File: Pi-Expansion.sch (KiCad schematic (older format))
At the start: 14 parts, among them J1 RPi_GPIO, J2 MMCX_H, P1 BATT, U1 A2200-A, U2 SPX2920U-5.0

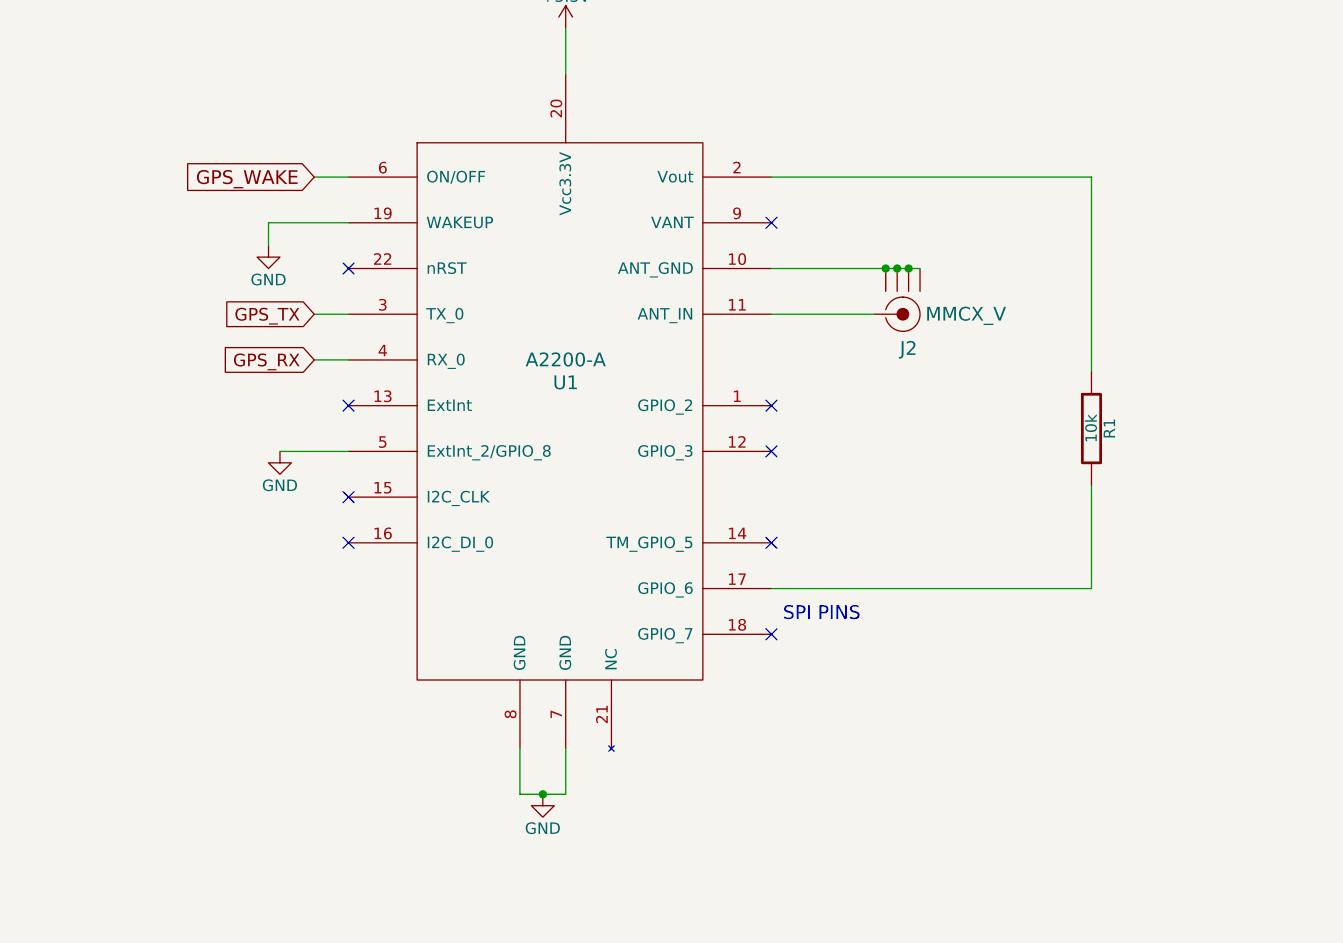
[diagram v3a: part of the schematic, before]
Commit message: Updated layout around gps, reconfigured for autowakeup and NMEA at 4800.
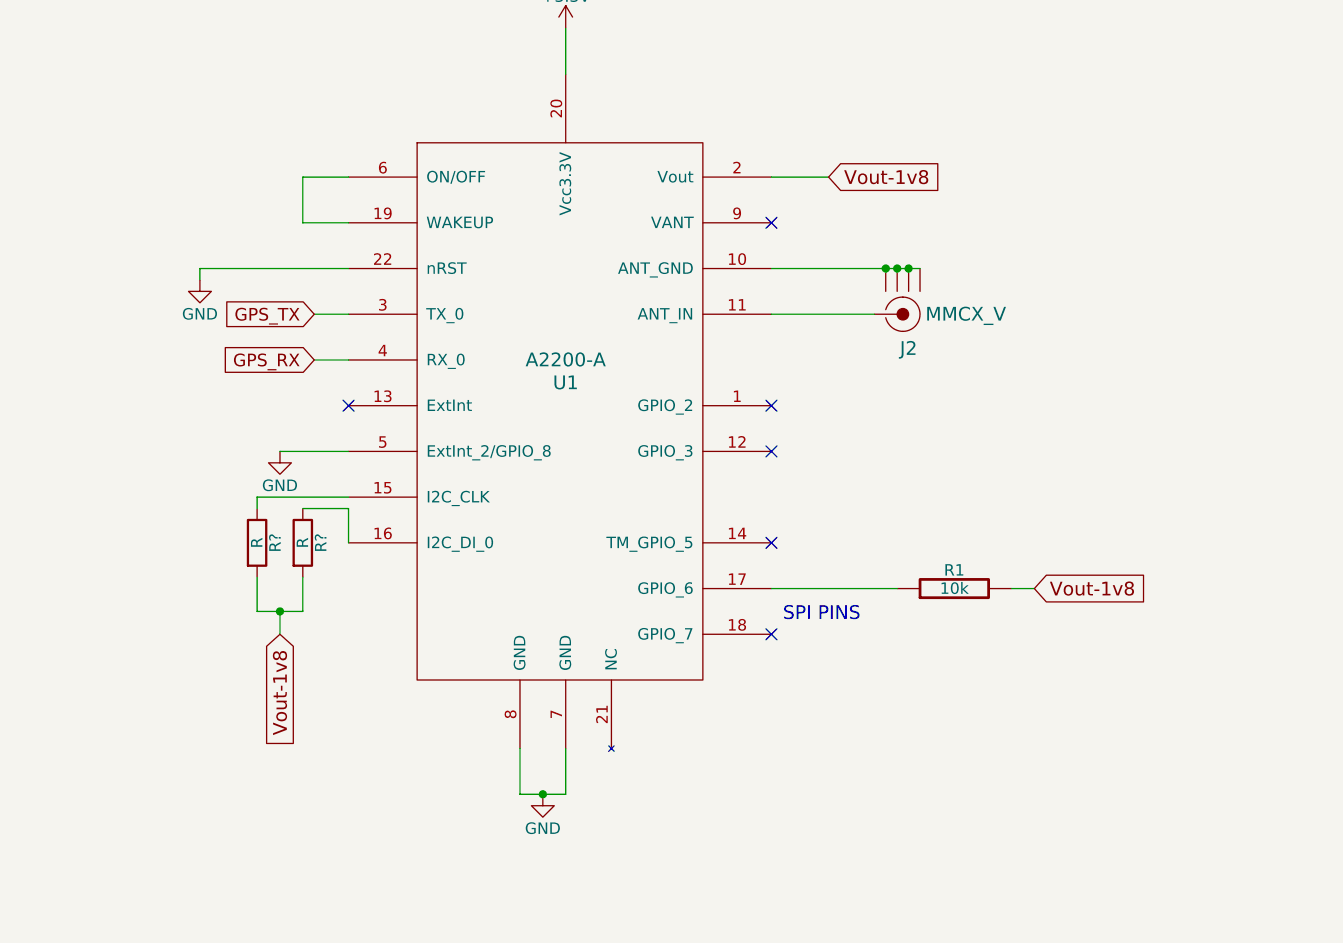
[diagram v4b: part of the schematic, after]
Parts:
- added R? (x2): R, symbol R
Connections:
- net GND: now also U1.22 (nRST); no longer U1.19 (WAKEUP)
- net GPS_WAKE: no longer U1.6 (ON/OFF)
- net at U1.15 (I2C_CLK): now also R?.1
- net at U1.16 (I2C_DI_0): now also R?.1
- net at U1.17 (GPIO_6): now also R1.1; no longer R1.2
- net Vout-1v8: now reaches U1.2 (Vout)
- net Vout-1v8: now also R1.2, R?.2, R?.2; no longer R1.1
- new net: U1.19 (WAKEUP), U1.6 (ON/OFF)
- no-connect marks 29 -> 26
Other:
- moved on the sheet: R1
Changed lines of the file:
@@
 L R-RESCUE-Pi-Expansion R1
 U 1 1 56C04659
-P 5650 2600
-F 0 "R1" V 5730 2600 50  0000 C CNN
-F 1 "10k" V 5650 2600 50  0000 C CNN
-F 2 "FT:1206" H 5650 2600 60  0001 C CNN
-F 3 "" H 5650 2600 60  0000 C CNN
-	1    5650 2600
-	1    0    0    -1
+P 5050 3300
+F 0 "R1" V 5130 3300 50  0000 C CNN
+F 1 "10k" V 5050 3300 50  0000 C CNN
+F 2 "FT:1206" H 5050 3300 60  0001 C CNN
+F 3 "" H 5050 3300 60  0000 C CNN
+	1    5050 3300
+	0    -1   -1   0
 $EndComp
 Wire Wire Line
@@
 Wire Wire Line
 	2100 2700 2400 2700
-Wire Wire Line
-	4250 1500 5650 1500
-Wire Wire Line
-	5650 1500 5650 2350
-Wire Wire Line
-	4250 3300 5650 3300
-Wire Wire Line
-	5650 3300 5650 2850
 Text Notes 4300 3450 0    60   ~ 0
 SPI PINS
@@
 NoConn ~ 4250 2500
 NoConn ~ 2400 2500
-NoConn ~ 2400 2900
-NoConn ~ 2400 3100
 NoConn ~ 4250 1700
 NoConn ~ 3400 5400
-NoConn ~ 2400 1900
 Text GLabel 3750 5700 2    60   Input ~ 0
 GPS_WAKE
 Wire Wire Line
 	3400 5700 3750 5700
-Text GLabel 2250 1500 0    60   Input ~ 0
-GPS_WAKE
-Wire Wire Line
-	2400 1500 2250 1500
-$Comp
-L GND #PWR010
-U 1 1 56C26D35
-P 2050 1800
-F 0 "#PWR010" H 2050 1550 50  0001 C CNN
-F 1 "GND" H 2050 1650 50  0000 C CNN
-F 2 "" H 2050 1800 50  0000 C CNN
-F 3 "" H 2050 1800 50  0000 C CNN
-	1    2050 1800
-	1    0    0    -1
-$EndComp
-Wire Wire Line
-	2050 1800 2050 1700
-Wire Wire Line
-	2050 1700 2400 1700
 NoConn ~ 1500 5900
 NoConn ~ 1500 5800
@@
 Wire Wire Line
 	8750 1450 9800 1450
+Wire Wire Line
+	2400 1700 2200 1700
+Wire Wire Line
+	2200 1700 2200 1500
+Wire Wire Line
+	2200 1500 2400 1500
+$Comp
+L R R?
+U 1 1 573A3BBE
+P 2200 3100
+F 0 "R?" V 2280 3100 50  0000 C CNN
+F 1 "R" V 2200 3100 50  0000 C CNN
+F 2 "" V 2130 3100 50  0000 C CNN
+F 3 "" H 2200 3100 50  0000 C CNN
+	1    2200 3100
+	1    0    0    -1
+$EndComp
+$Comp
+L R R?
+U 1 1 573A3C2D
+P 2000 3100
+F 0 "R?" V 2080 3100 50  0000 C CNN
+F 1 "R" V 2000 3100 50  0000 C CNN
+F 2 "" V 1930 3100 50  0000 C CNN
+F 3 "" H 2000 3100 50  0000 C CNN
+	1    2000 3100
+	1    0    0    -1
+$EndComp
+Wire Wire Line
+	2400 2900 2000 2900
+Wire Wire Line
+	2000 2900 2000 2950
+Wire Wire Line
+	2400 3100 2400 2950
+Wire Wire Line
+	2400 2950 2200 2950
+Wire Wire Line
+	2000 3250 2000 3400
+Wire Wire Line
+	2000 3400 2200 3400
+Wire Wire Line
+	2200 3400 2200 3250
+Text GLabel 2100 3500 3    60   Input ~ 0
+Vout-1v8
+Text GLabel 4500 1500 2    60   Input ~ 0
+Vout-1v8
+Text GLabel 5400 3300 2    60   Input ~ 0
+Vout-1v8
+Wire Wire Line
+	2100 3500 2100 3400
+Connection ~ 2100 3400
+Wire Wire Line
+	4250 1500 4500 1500
+Wire Wire Line
+	4250 3300 4800 3300
+Wire Wire Line
+	5300 3300 5400 3300
+$Comp
+L GND #PWR?
+U 1 1 573A4B6B
+P 1750 1950
+F 0 "#PWR?" H 1750 1700 50  0001 C CNN
+F 1 "GND" H 1750 1800 50  0000 C CNN
+F 2 "" H 1750 1950 50  0000 C CNN
+F 3 "" H 1750 1950 50  0000 C CNN
+	1    1750 1950
+	1    0    0    -1
+$EndComp
+Wire Wire Line
+	2400 1900 1750 1900
+Wire Wire Line
+	1750 1900 1750 1950
 $EndSCHEMATC

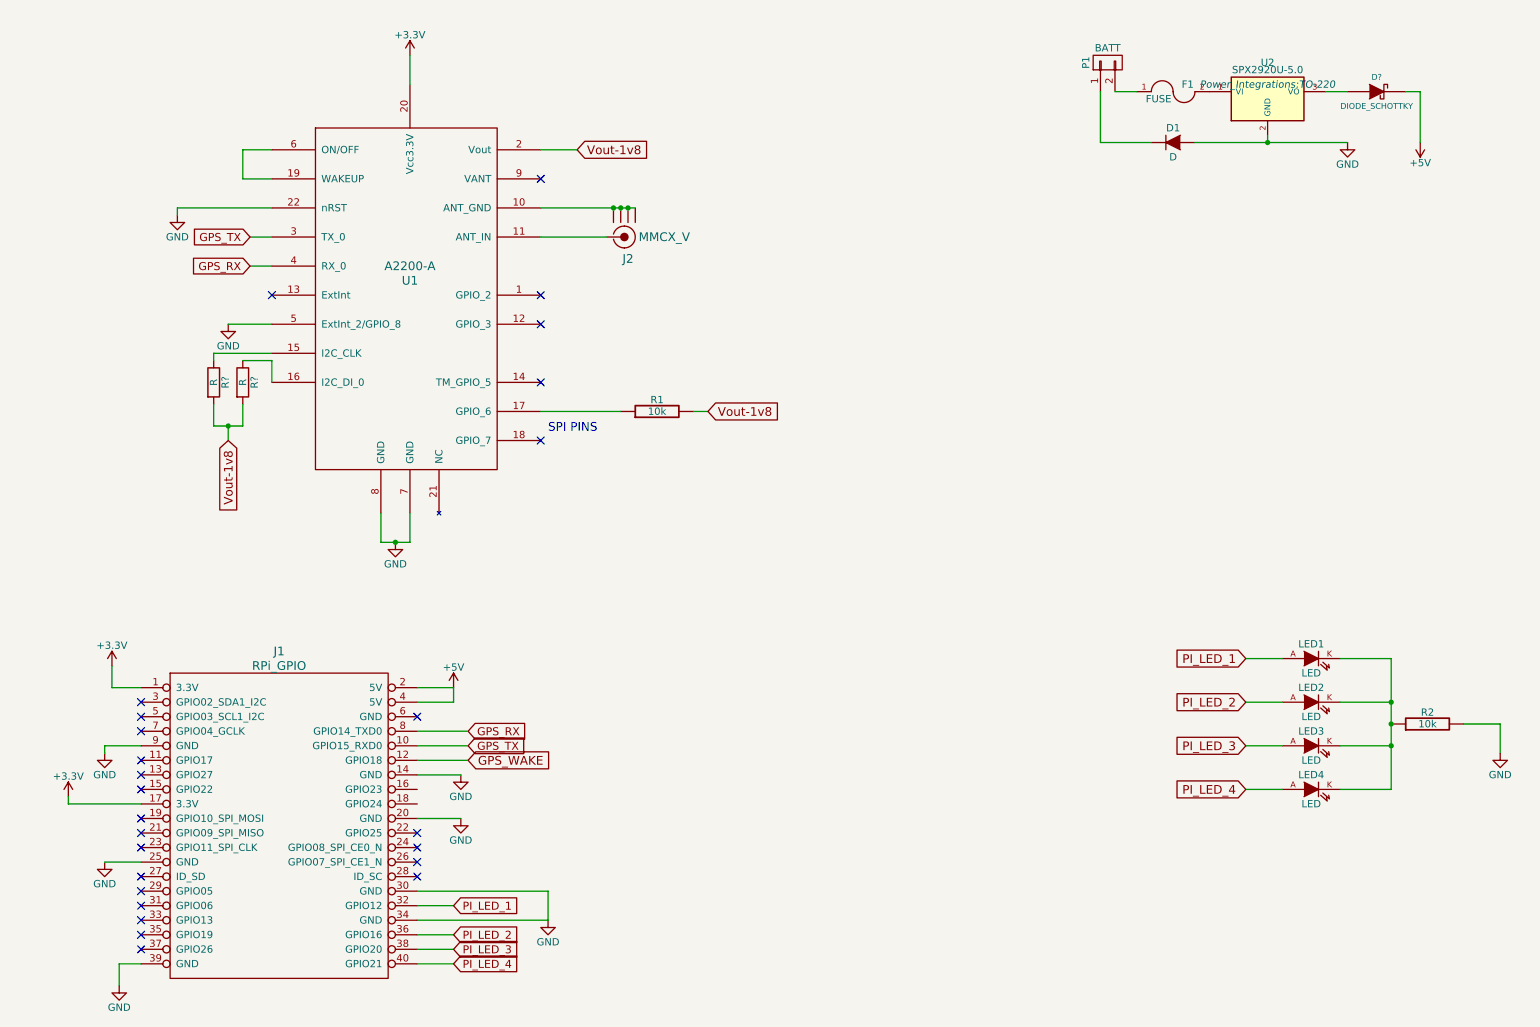
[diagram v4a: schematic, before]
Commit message: minor tweaks, and rotated pi header, removed infill and traces
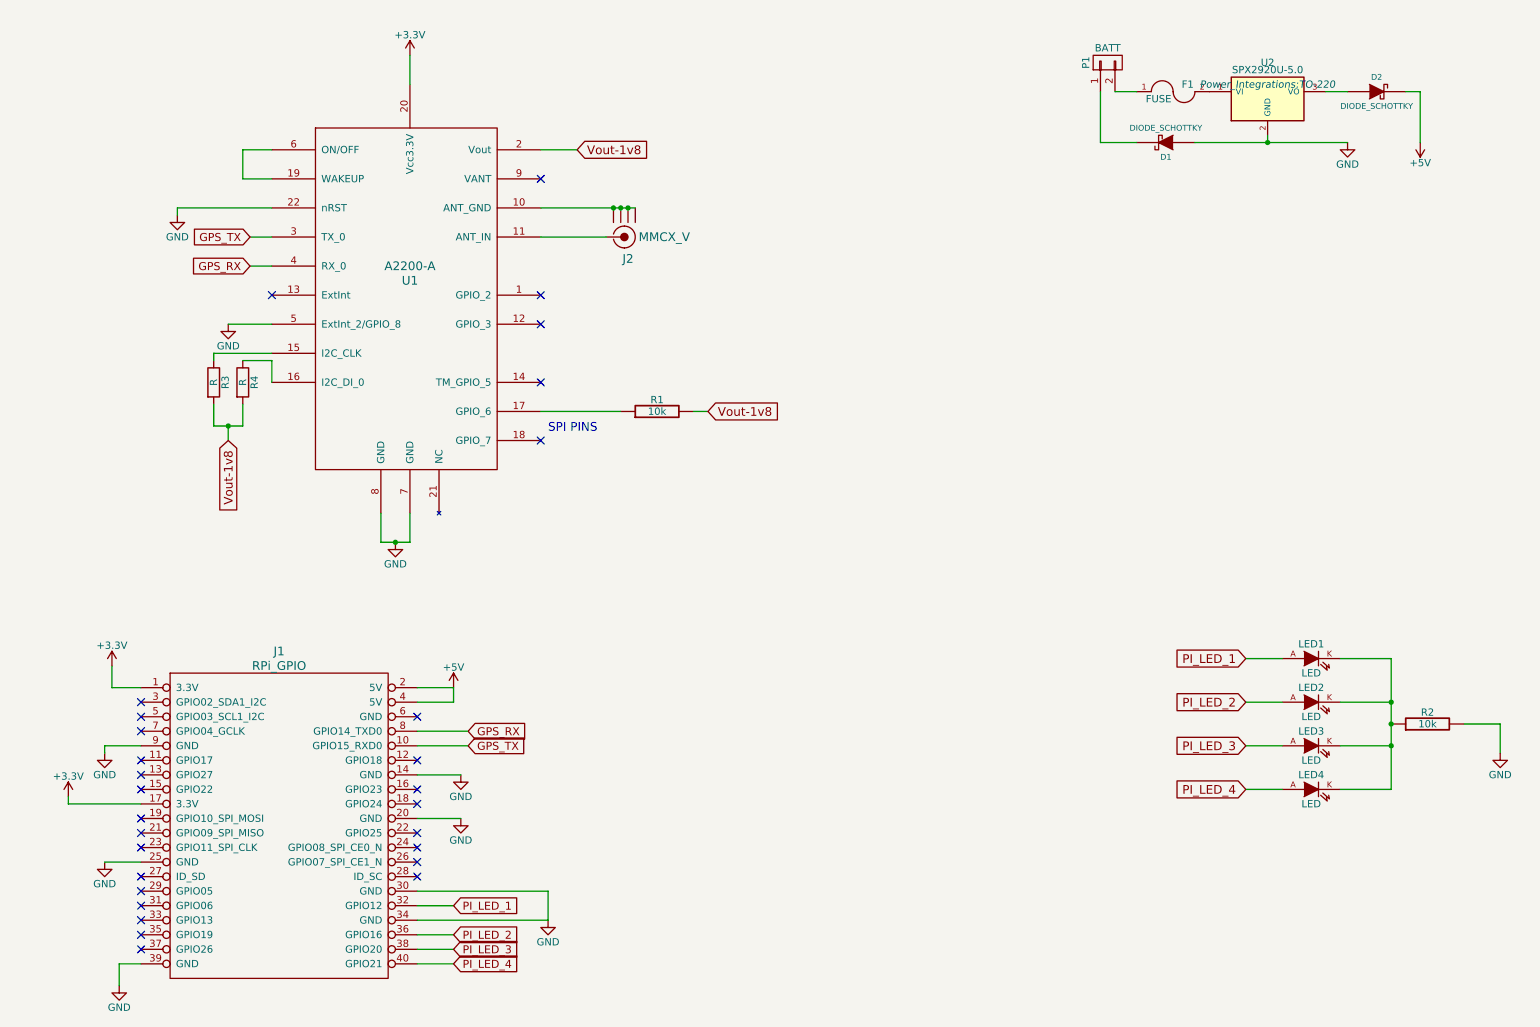
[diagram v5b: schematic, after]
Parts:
- removed D1: D, Diodes_ThroughHole:Diode_DO-41_SOD81_Horizontal_RM10, symbol D
- added D1: DIODE_SCHOTTKY, symbol DIODE_SCHOTTKY
- gave numbers to parts that had none: 3
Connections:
- net GND: now also D1.A
- net at P1.1 (P1): now also D1.K
- net GPS_WAKE: no longer names the net of J1.12 (GPIO18)
- no-connect marks 26 -> 29
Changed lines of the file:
@@
 $EndComp
 $Comp
-L GND #PWR01
+L GND #PWR16
 U 1 1 56C02961
 P 10850 5650
-F 0 "#PWR01" H 10850 5400 50  0001 C CNN
+F 0 "#PWR16" H 10850 5400 50  0001 C CNN
 F 1 "GND" H 10850 5500 50  0000 C CNN
 F 2 "" H 10850 5650 50  0000 C CNN
@@
 $EndComp
 $Comp
-L GND #PWR02
+L GND #PWR5
 U 1 1 56C0368B
 P 1350 7250
-F 0 "#PWR02" H 1350 7000 50  0001 C CNN
+F 0 "#PWR5" H 1350 7000 50  0001 C CNN
 F 1 "GND" H 1350 7100 50  0000 C CNN
 F 2 "" H 1350 7250 50  0000 C CNN
@@
 $EndComp
 $Comp
-L GND #PWR03
+L GND #PWR8
 U 1 1 56C036F9
 P 3250 4200
-F 0 "#PWR03" H 3250 3950 50  0001 C CNN
+F 0 "#PWR8" H 3250 3950 50  0001 C CNN
 F 1 "GND" H 3250 4050 50  0000 C CNN
 F 2 "" H 3250 4200 50  0000 C CNN
@@
 $EndComp
 $Comp
-L +3.3V #PWR04
+L +3.3V #PWR9
 U 1 1 56C03A1A
 P 3350 850
-F 0 "#PWR04" H 3350 700 50  0001 C CNN
+F 0 "#PWR9" H 3350 700 50  0001 C CNN
 F 1 "+3.3V" H 3350 990 50  0000 C CNN
 F 2 "" H 3350 850 50  0000 C CNN
@@
 PI_LED_4
 $Comp
-L GND #PWR05
+L GND #PWR7
 U 1 1 56C04494
 P 2100 2700
-F 0 "#PWR05" H 2100 2450 50  0001 C CNN
+F 0 "#PWR7" H 2100 2450 50  0001 C CNN
 F 1 "GND" H 2100 2550 50  0000 C CNN
 F 2 "" H 2100 2700 50  0000 C CNN
@@
 $EndComp
 $Comp
-L +5V #PWR06
+L +5V #PWR15
 U 1 1 56C07DE9
 P 10300 1450
-F 0 "#PWR06" H 10300 1300 50  0001 C CNN
+F 0 "#PWR15" H 10300 1300 50  0001 C CNN
 F 1 "+5V" H 10300 1590 50  0000 C CNN
 F 2 "" H 10300 1450 50  0000 C CNN
@@
 	10300 1100 10300 1450
 $Comp
-L +5V #PWR07
+L +5V #PWR10
 U 1 1 56C0814E
 P 3650 5200
-F 0 "#PWR07" H 3650 5050 50  0001 C CNN
+F 0 "#PWR10" H 3650 5050 50  0001 C CNN
 F 1 "+5V" H 3650 5340 50  0000 C CNN
 F 2 "" H 3650 5200 50  0000 C CNN
@@
 	3400 5200 3650 5200
 $Comp
-L +3.3V #PWR08
+L +3.3V #PWR4
 U 1 1 56C085CB
 P 1300 5050
-F 0 "#PWR08" H 1300 4900 50  0001 C CNN
+F 0 "#PWR4" H 1300 4900 50  0001 C CNN
 F 1 "+3.3V" H 1300 5190 50  0000 C CNN
 F 2 "" H 1300 5050 50  0000 C CNN
@@
 	1300 5200 1500 5200
 $Comp
-L GND #PWR09
+L GND #PWR14
 U 1 1 56C08732
 P 9800 1450
-F 0 "#PWR09" H 9800 1200 50  0001 C CNN
+F 0 "#PWR14" H 9800 1200 50  0001 C CNN
 F 1 "GND" H 9800 1300 50  0000 C CNN
 F 2 "" H 9800 1450 50  0000 C CNN
@@
 	8200 1100 8350 1100
 Wire Wire Line
-	8100 1450 8450 1450
-Wire Wire Line
 	8100 1450 8100 1100
-$Comp
-L D D1
-U 1 1 56C23E17
-P 8600 1450
-F 0 "D1" H 8600 1550 50  0000 C CNN
-F 1 "D" H 8600 1350 50  0000 C CNN
-F 2 "Diodes_ThroughHole:Diode_DO-41_SOD81_Horizontal_RM10" H 8600 1450 50  0001 C CNN
-F 3 "" H 8600 1450 50  0000 C CNN
-	1    8600 1450
-	1    0    0    -1
-$EndComp
 NoConn ~ 3400 6500
 NoConn ~ 3400 6400
@@
 NoConn ~ 4250 1700
 NoConn ~ 3400 5400
-Text GLabel 3750 5700 2    60   Input ~ 0
-GPS_WAKE
-Wire Wire Line
-	3400 5700 3750 5700
 NoConn ~ 1500 5900
 NoConn ~ 1500 5800
@@
 NoConn ~ 1500 5500
 $Comp
-L GND #PWR?
+L GND #PWR2
 U 1 1 573A1DF2
 P 1250 5650
-F 0 "#PWR?" H 1250 5400 50  0001 C CNN
+F 0 "#PWR2" H 1250 5400 50  0001 C CNN
 F 1 "GND" H 1250 5500 50  0000 C CNN
 F 2 "" H 1250 5650 50  0000 C CNN
@@
 $EndComp
 $Comp
-L +3.3V #PWR?
+L +3.3V #PWR1
 U 1 1 573A1E20
 P 1000 5950
-F 0 "#PWR?" H 1000 5800 50  0001 C CNN
+F 0 "#PWR1" H 1000 5800 50  0001 C CNN
 F 1 "+3.3V" H 1000 6090 50  0000 C CNN
 F 2 "" H 1000 5950 50  0000 C CNN
@@
 $EndComp
 $Comp
-L GND #PWR?
+L GND #PWR3
 U 1 1 573A1E4E
 P 1250 6400
-F 0 "#PWR?" H 1250 6150 50  0001 C CNN
+F 0 "#PWR3" H 1250 6150 50  0001 C CNN
 F 1 "GND" H 1250 6250 50  0000 C CNN
 F 2 "" H 1250 6400 50  0000 C CNN
@@
 $EndComp
 $Comp
-L GND #PWR?
+L GND #PWR11
 U 1 1 573A1E7C
 P 3700 5800
-F 0 "#PWR?" H 3700 5550 50  0001 C CNN
+F 0 "#PWR11" H 3700 5550 50  0001 C CNN
 F 1 "GND" H 3700 5650 50  0000 C CNN
 F 2 "" H 3700 5800 50  0000 C CNN
@@
 $EndComp
 $Comp
-L GND #PWR?
+L GND #PWR12
 U 1 1 573A1EAA
 P 3700 6100
-F 0 "#PWR?" H 3700 5850 50  0001 C CNN
+F 0 "#PWR12" H 3700 5850 50  0001 C CNN
 F 1 "GND" H 3700 5950 50  0000 C CNN
 F 2 "" H 3700 6100 50  0000 C CNN
@@
 $EndComp
 $Comp
-L GND #PWR?
+L GND #PWR13
 U 1 1 573A1ED8
 P 4300 6800
-F 0 "#PWR?" H 4300 6550 50  0001 C CNN
+F 0 "#PWR13" H 4300 6550 50  0001 C CNN
 F 1 "GND" H 4300 6650 50  0000 C CNN
 F 2 "" H 4300 6800 50  0000 C CNN
@@
 	3650 5300 3650 5200
 $Comp
-L DIODE_SCHOTTKY D?
+L DIODE_SCHOTTKY D2
 U 1 1 573A3154
 P 10000 1100
-F 0 "D?" H 10000 1200 40  0000 C CNN
+F 0 "D2" H 10000 1200 40  0000 C CNN
 F 1 "DIODE_SCHOTTKY" H 10000 1000 40  0000 C CNN
 F 2 "" H 10000 1100 60  0000 C CNN
@@
 	2200 1500 2400 1500
 $Comp
-L R R?
+L R R4
 U 1 1 573A3BBE
 P 2200 3100
-F 0 "R?" V 2280 3100 50  0000 C CNN
+F 0 "R4" V 2280 3100 50  0000 C CNN
 F 1 "R" V 2200 3100 50  0000 C CNN
 F 2 "" V 2130 3100 50  0000 C CNN
@@
 $EndComp
 $Comp
-L R R?
+L R R3
 U 1 1 573A3C2D
 P 2000 3100
-F 0 "R?" V 2080 3100 50  0000 C CNN
+F 0 "R3" V 2080 3100 50  0000 C CNN
 F 1 "R" V 2000 3100 50  0000 C CNN
 F 2 "" V 1930 3100 50  0000 C CNN
@@
 	5300 3300 5400 3300
 $Comp
-L GND #PWR?
+L GND #PWR6
 U 1 1 573A4B6B
 P 1750 1950
-F 0 "#PWR?" H 1750 1700 50  0001 C CNN
+F 0 "#PWR6" H 1750 1700 50  0001 C CNN
 F 1 "GND" H 1750 1800 50  0000 C CNN
 F 2 "" H 1750 1950 50  0000 C CNN
@@
 Wire Wire Line
 	1750 1900 1750 1950
+NoConn ~ 3400 5700
+NoConn ~ 3400 5900
+NoConn ~ 3400 6000
+$Comp
+L DIODE_SCHOTTKY D1
+U 1 1 573A5A31
+P 8550 1450
+F 0 "D1" H 8550 1550 40  0000 C CNN
+F 1 "DIODE_SCHOTTKY" H 8550 1350 40  0000 C CNN
+F 2 "" H 8550 1450 60  0000 C CNN
+F 3 "" H 8550 1450 60  0000 C CNN
+	1    8550 1450
+	-1   0    0    1
+$EndComp
+Wire Wire Line
+	8100 1450 8350 1450
 $EndSCHEMATC
